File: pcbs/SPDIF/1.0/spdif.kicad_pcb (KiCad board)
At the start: 4 copper layers, 85 x 55 mm, 67 parts, among them J1 Conn_01x02_Pin, J10 Conn_01x05_Pin, J11 Conn_01x04_Pin, J12 Conn_01x03_Pin, J13 Conn_01x02_Pin, J2 Conn_01x02_Pin, J3 Conn_01x02_Pin, J4 Conn_01x02_Pin, J5 Conn_01x02_Pin, J6 Conn_01x04_Pin, J7 Conn_01x04_Pin, J8 Conn_01x04_Pin, J9 Conn_01x02_Pin, U1 DA101C_C6931652, U2 DA101C_C6931652, U3 DA101C_C6931652, U4 DA101C_C6931652, U5 74HC7014, U6 DIX9211, U7 AMS1117-3.3, Y1 24.576MHz

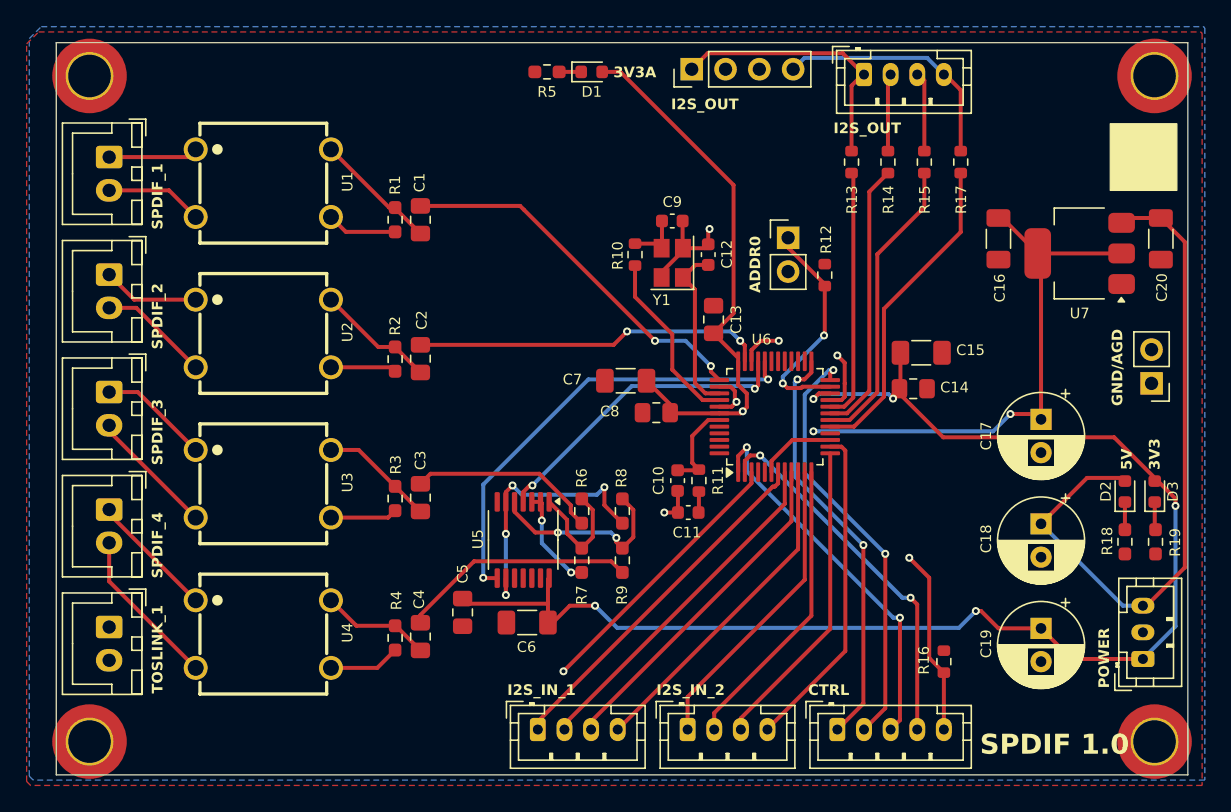
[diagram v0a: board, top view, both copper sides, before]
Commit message: Updated screenshots
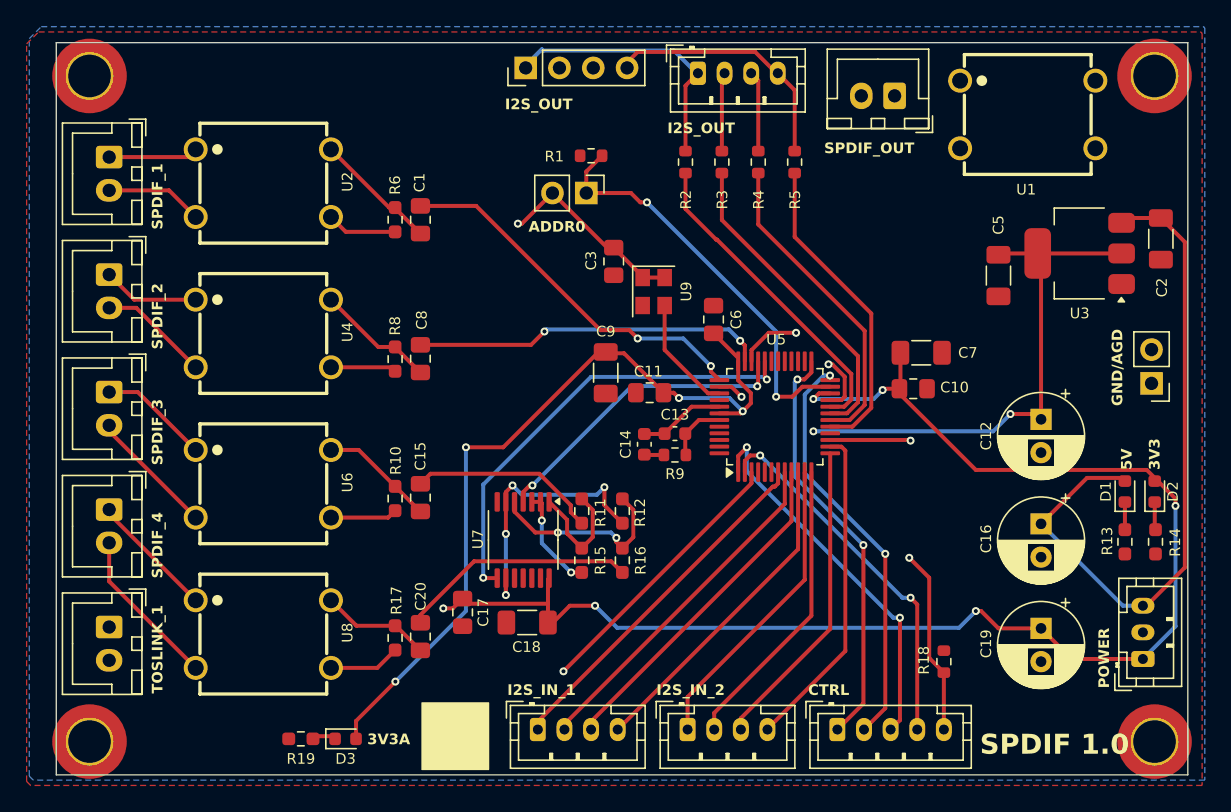
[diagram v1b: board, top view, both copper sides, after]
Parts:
- removed the C12 at (75.3, 44.2)
- removed the C9 at (72.6, 41.7)
- removed the R10 at (69.8, 44.2)
- removed Y1: 24.576MHz, Crystal:Crystal_SMD_SeikoEpson_FA238-4Pin_3.2x2.5mm
- added C3: 0.1u, Capacitor_SMD:C_0805_2012Metric_Pad1.18x1.45mm_HandSolder, F.Cu at (68.2, 44.7)
- added J3: Conn_01x02_Pin, Connector_JST:JST_XH_B2B-XH-A_1x02_P2.50mm_Vertical, F.Cu at (89.3, 32.3)
- added U1: DA101C_C6931652, easyeda2kicad:XFMR-TH_4P-L9.5-W9.0-P5.08-LS10.2_C9900096976, F.Cu at (99.3, 33.7)
- added U9: ASDMB-xxxMHz, Oscillator:Oscillator_SMD_Abracon_ASE-4Pin_3.2x2.5mm, F.Cu at (71.2, 47.0)
- moved D3 53.4 mm to (48.1, 80.6)
- moved R19 53.4 mm to (44.7, 80.6)
- moved R1 19.7 mm to (66.5, 36.8), turned to 0 degrees
- moved J5 15.5 mm to (66.1, 39.6), turned to -90 degrees
- moved J1 12.5 mm to (61.6, 30.2)
- moved J2 12.5 mm to (74.5, 30.6)
- moved R2 12.5 mm to (73.6, 37.3)
- moved R3 12.5 mm to (76.3, 37.3)
- moved R4 12.5 mm to (79.1, 37.3)
- moved R5 12.5 mm to (81.8, 37.3)
- moved C14 6.10 mm to (70.5, 58.5), turned to -90 degrees
- moved C13 3.53 mm to (72.8, 57.7), turned to 0 degrees
- moved C5 2.76 mm to (97.1, 45.8)
- moved R9 2.64 mm to (72.8, 59.3), turned to 180 degrees
- moved C9 1.62 mm to (67.6, 53.1), turned to 90 degrees
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- renumbered C14 to C10, C8 to C11, C17 to C12, C10 to C13, C11 to C14, C3 to C15, C18 to C16, C5 to C17, C6 to C18, C20 to C2, C4 to C20, C16 to C5, C13 to C6, C15 to C7, C2 to C8, C7 to C9, D2 to D1, D3 to D2, D1 to D3, H3 to H2, H2 to H3, J8 to J1, J5 to J10, J12 to J11, J6 to J12, J7 to J13, J10 to J14, J11 to J2, J1 to J4, J9 to J5, J2 to J6, J13 to J7, J3 to J8, J4 to J9, R12 to R1, R3 to R10, R6 to R11, R8 to R12, R18 to R13, R19 to R14, R7 to R15, R9 to R16, R4 to R17, R16 to R18, R5 to R19, R13 to R2, R14 to R3, R15 to R4, R17 to R5, R1 to R6, R2 to R8, R11 to R9, U1 to U2, U7 to U3, U2 to U4, U6 to U5, U3 to U6, U5 to U7, U4 to U8
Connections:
- C13 pad 1: AGND -> FILTGND
- C14 pad 1: AGND -> FILTGND
- U5 pad 40: XTO -> unconnected-(U5-XTO-Pad40)
- U5 pad 41: AGND -> FILTGND
- U5 pad 6: SPDIF_OUT -> unconnected-(U5-MPIO_A3-Pad6)
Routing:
- net 3V3: track 116.5 -> 152.5 mm, vias 5 -> 7
- net SPDIF_OUT: track 5.44 -> 38.7 mm, vias 0 -> 1
- net 3V3A: track 85.8 -> 103.9 mm, vias 3 -> 6
- net ADR0: track 17.1 -> 31.1 mm
- net XTO: track 13.5 -> 0.00 mm
- net AGND: track 34.4 -> 22.2 mm, vias 3 -> 1
- net SPDIFPOS: track 0.00 -> 8.68 mm
- net FILTGND: track 0.00 -> 6.55 mm
- net SPDIFNEG: track 0.00 -> 6.51 mm
- net Net-(U5-SCLKO): track 18.9 -> 24.0 mm
- net XTI: track 12.7 -> 8.80 mm
- net Net-(C9-Pad1): track 3.67 -> 0.00 mm
- net Net-(U5-BCLK): track 20.6 -> 23.9 mm
- net Net-(U5-FILT): track 6.82 -> 4.54 mm
- net SPDIF_RESET: track 37.5 -> 39.1 mm
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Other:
- board text added: "SPDIF_OUT"
